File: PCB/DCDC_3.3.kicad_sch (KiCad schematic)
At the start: 16 parts, among them U10 LV2842XLVDDCR

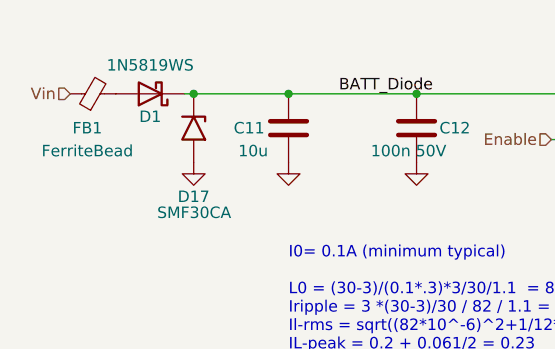
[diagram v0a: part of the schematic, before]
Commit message: Schootky reverse voltage protection replaced with switching diode to make there is no reverse current
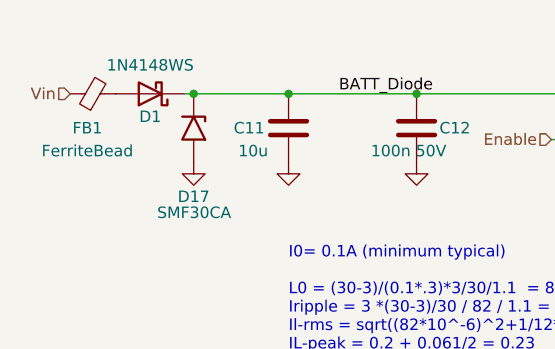
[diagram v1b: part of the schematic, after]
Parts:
- D1: value 1N5819WS -> 1N4148WS; LCSC C191023 -> C2128
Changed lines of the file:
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@@
       (effects (font (size 1.27 1.27)))
     )
-    (property "Value" "1N5819WS" (at 63.373 42.037 0)
+    (property "Value" "1N4148WS" (at 63.373 42.037 0)
       (effects (font (size 1.27 1.27)))
     )
@@
       (effects (font (size 1.27 1.27)) hide)
     )
-    (property "Datasheet" "https://datasheet.lcsc.com/lcsc/2204281430_Guangdong-Hottech-1N5819WS_C191023.pdf" (at 63.373 45.212 0)
+    (property "Datasheet" "https://datasheet.lcsc.com/lcsc/1810101110_Jiangsu-Changjing-Electronics-Technology-Co---Ltd--1N4148WS_C2128.pdf" (at 63.373 45.212 0)
       (effects (font (size 1.27 1.27)) hide)
     )
-    (property "LCSC" "C191023" (at 63.6905 38.227 0)
+    (property "LCSC" "C2128" (at 63.6905 38.227 0)
       (effects (font (size 1.27 1.27)) hide)
     )

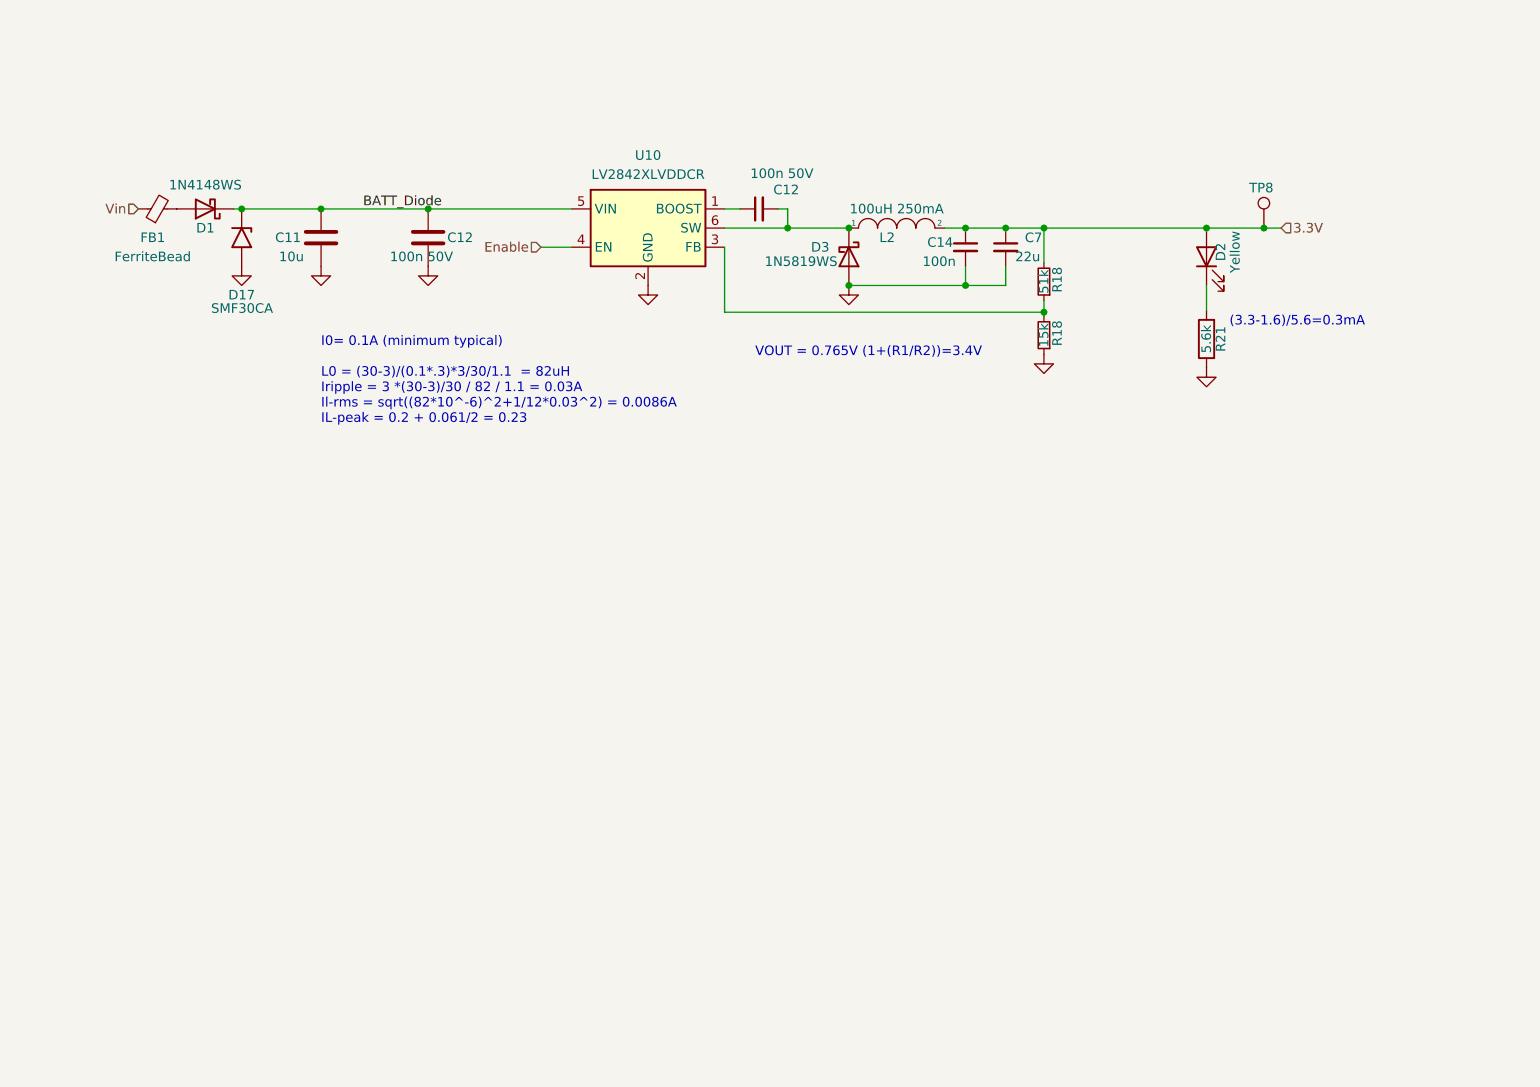
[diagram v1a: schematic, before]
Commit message: P-channel aux load switching pullup (normally opened). Optional disabling of DCDC
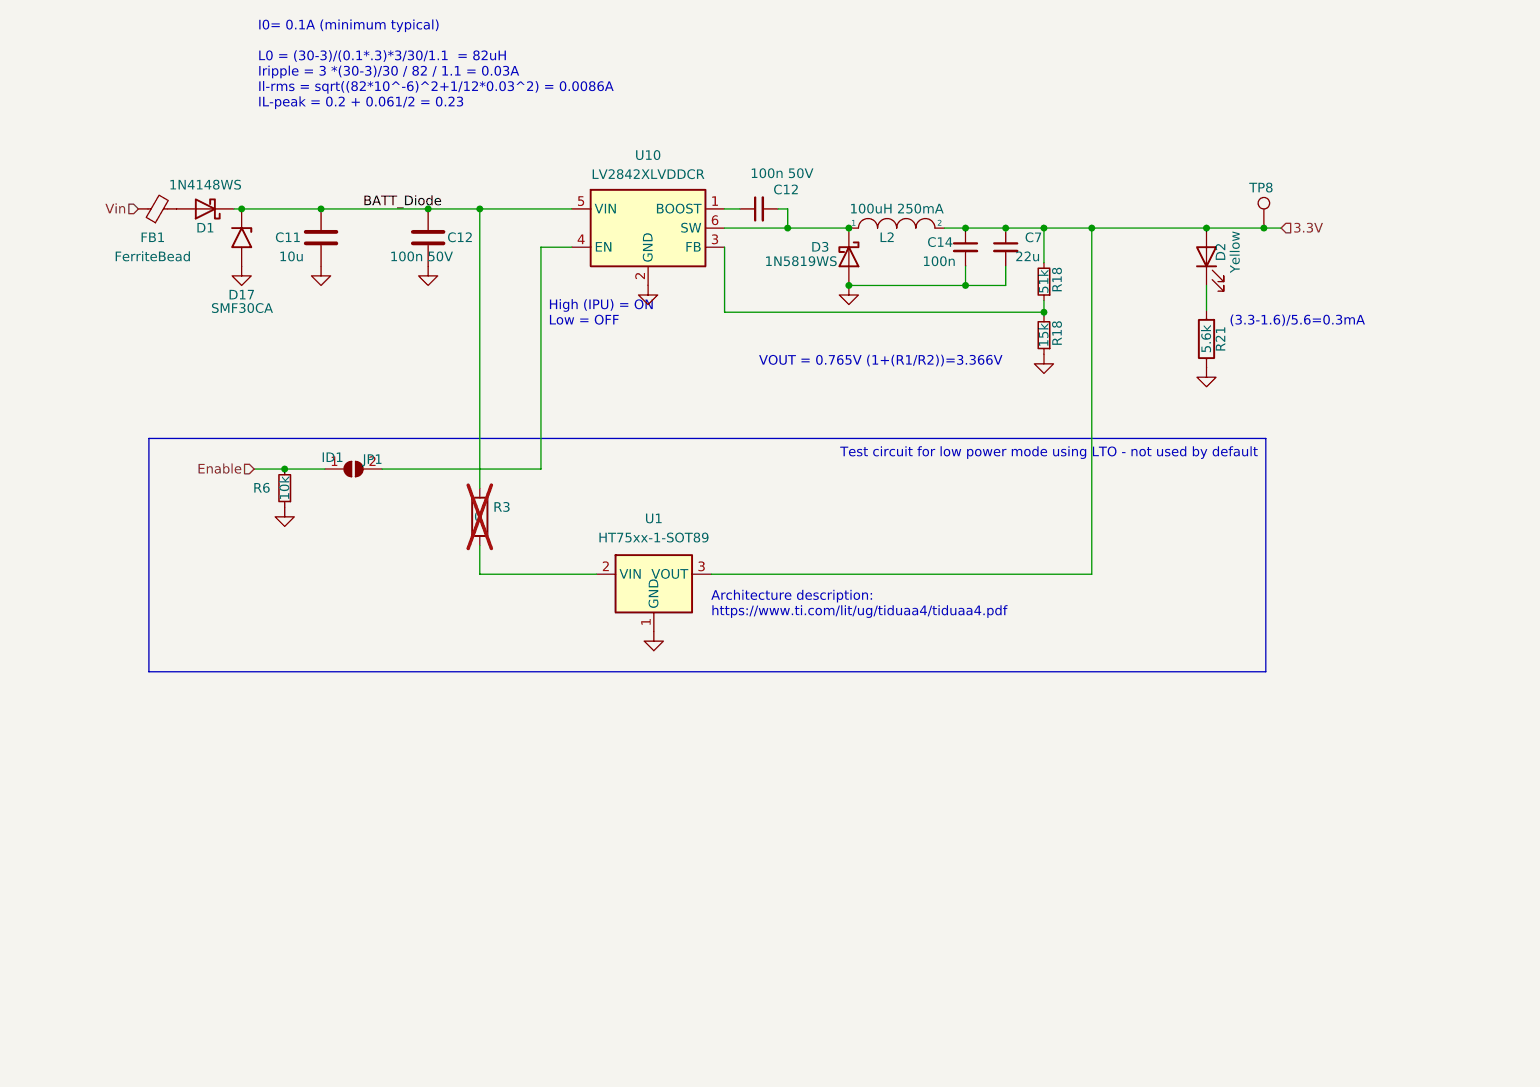
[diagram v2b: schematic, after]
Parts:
- added JP1: ID1, Jumper:SolderJumper-2_P1.3mm_Open_RoundedPad1.0x1.5mm, symbol Jumper:SolderJumper_2_Open
- added R3: 0, Resistor_SMD:R_0805_2012Metric, symbol Device:R
- added R6: 10k, Resistor_SMD:R_0402_1005Metric, symbol Device:R_Small
- added U1: HT75xx-1-SOT89, Package_TO_SOT_SMD:SOT-89-3, symbol Regulator_Linear:HT75xx-1-SOT89
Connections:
- net 3.3V: now also U1.3 (VOUT)
- net BATT_Diode: now also R3.1
- net Enable: now also JP1.1 (A), R6.2; no longer U10.4 (EN)
- net GND: now also R6.1, U1.1 (GND)
- new net: JP1.2 (B), U10.4 (EN)
- new net: R3.2, U1.2 (VIN)
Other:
- note added: "Architecture description: https://www.ti.com/lit/ug/tiduaa4/tiduaa4.pdf"
- note added: "High (IPU) = ON Low = OFF"
- note added: "VOUT = 0.765V (1+(R1/R2))=3.366V"
- note removed: "VOUT = 0.765V (1+(R1/R2))=3.4V"

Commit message: Mosfets for load switchiong. DCDC Enable pin. Rerouting.
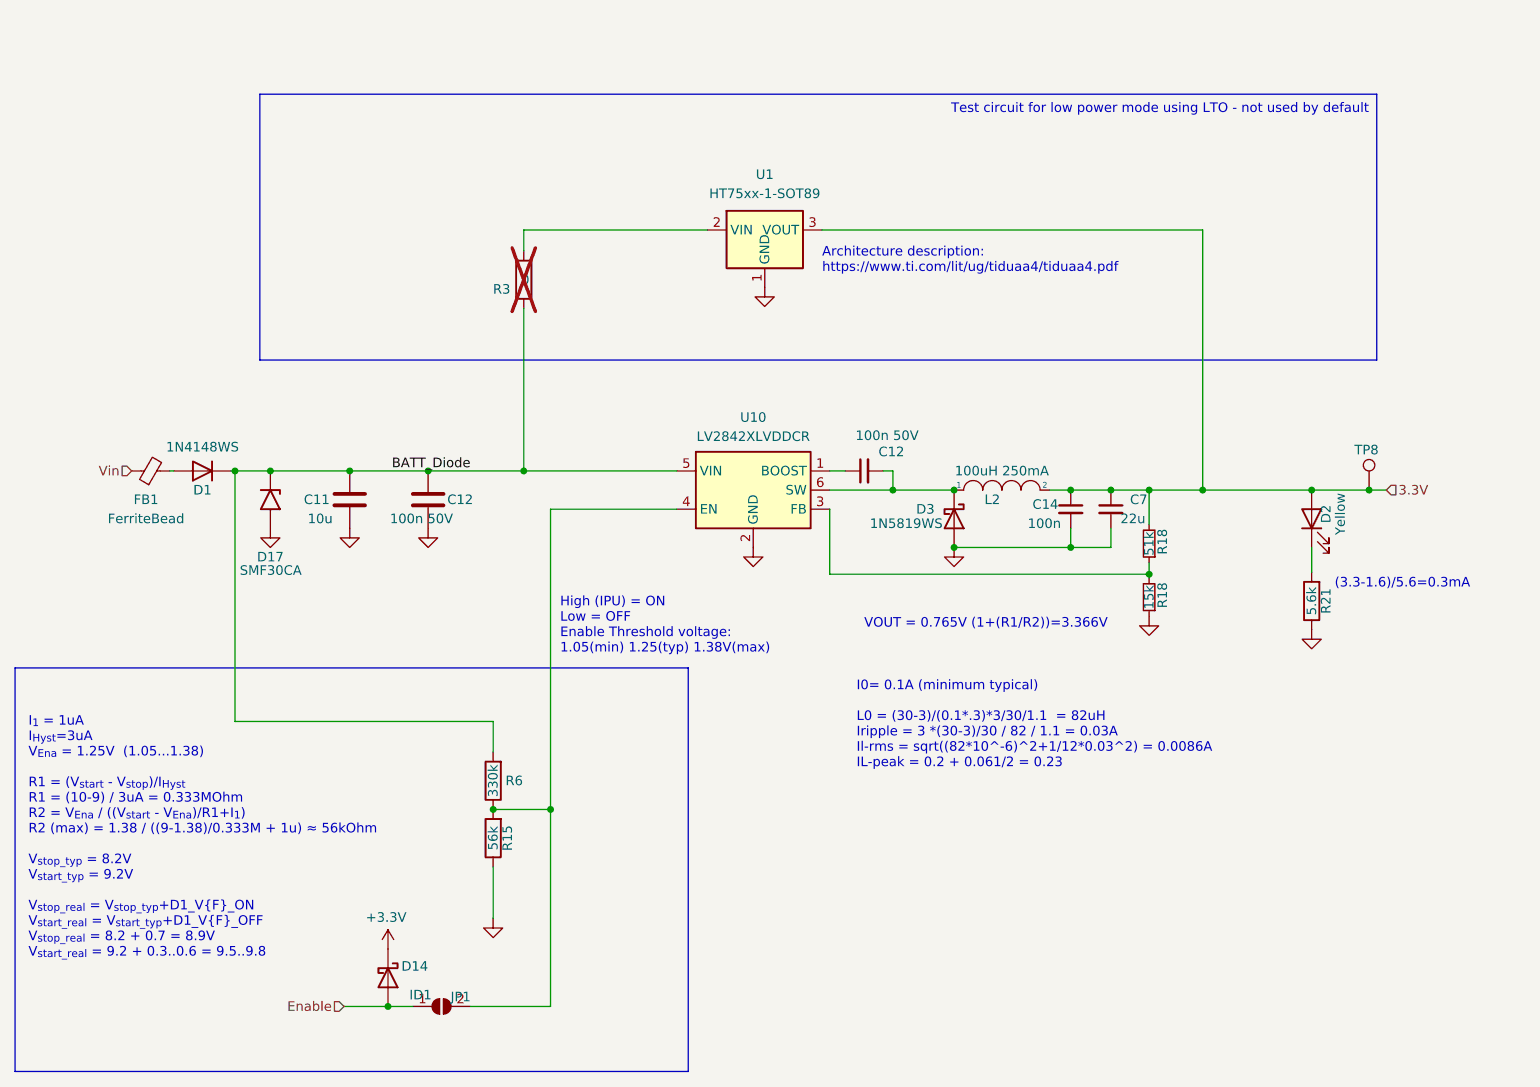
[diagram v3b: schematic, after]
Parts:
- removed R6: 10k, Resistor_SMD:R_0402_1005Metric, symbol Device:R_Small
- added D14: 1N5819WS, Diode_SMD:D_SOD-323, symbol Diode:1N5819
- added R15: 56k, Resistor_SMD:R_0402_1005Metric, symbol Device:R
- added R6: 330k, Resistor_SMD:R_0402_1005Metric, symbol Device:R
- D1: symbol Diode:1N5819 -> Diode:1N4148WS; Note (none) -> Low reverse current
- R3: LCSC (none) -> C21189; LSCS C21189 -> (none)
- U1: LCSC (none) -> C14289; LSCS C14289 -> (none)
- U10: Alternative LMR14010A or LMR14006 -> LMR14010A or LMR14006 or TPS54160; LCSC (none) -> C225807; LSCS C225807 -> (none)
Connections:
- net BATT_Diode: now also R6.2
- net Enable: now also D14.2 (A)
- net GND: now also R15.1
- net at JP1.2 (B), U10.4 (EN): now also R15.2, R6.1
- new net +3.3V: D14.1 (K)
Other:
- note added: "High (IPU) = ON Low = OFF Enable Threshold voltage: 1.05(min) 1.25(typ) 1.38V(max)"
- note added: "I_{1} = 1uA I_{Hyst}=3uA V_{Ena} = 1.25V (1.05...1.38) R1 = (V_{start} - V_{stop})/I_{Hyst} R1 = (10-9) / 3uA = 0.333MOhm R2 = V_{Ena} / ((V_{start} - V_{Ena})/R1+I_{1}) R2 (max) = 1.38 / ((9-1.38)/0.333M + 1u) ≈ 56kOhm V_{stop_typ} = 8.2V V_{start_typ} = 9.2V V_{stop_real} = V_{stop_typ}+D1_V{F}_ON V_{start_real} = V_{start_typ}+D1_V{F}_OFF V_{stop_real} = 8.2 + 0.7 = 8.9V V_{start_real} = 9.2 +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"
- note removed: "High (IPU) = ON Low = OFF"
- moved on the sheet: C11, C12, C14, C7, D1, D17, D2, D3, FB1, JP1, L2, R18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

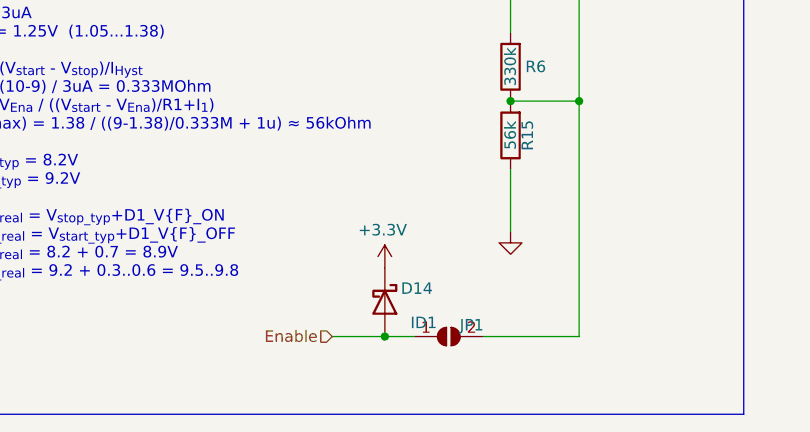
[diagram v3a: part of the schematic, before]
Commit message: DCDC force enable option
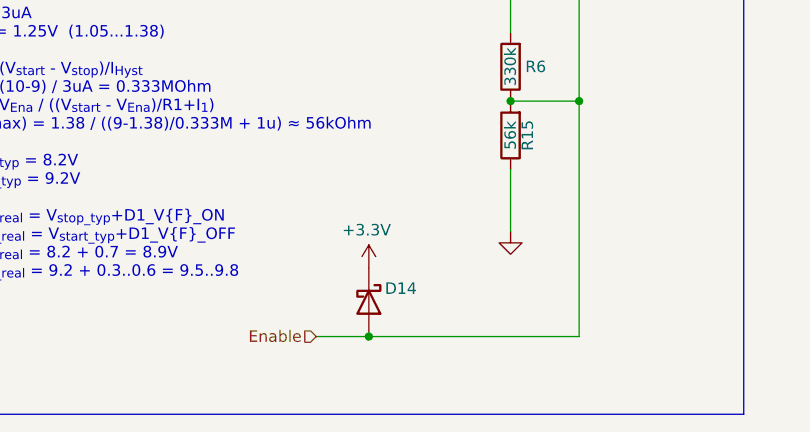
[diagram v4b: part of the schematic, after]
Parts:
- removed JP1: ID1, Jumper:SolderJumper-2_P1.3mm_Open_RoundedPad1.0x1.5mm, symbol Jumper:SolderJumper_2_Open
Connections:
- net Enable: now also R15.2, R6.1, U10.4 (EN)
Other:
- moved on the sheet: D14
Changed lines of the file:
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@@
   (junction (at 188.722 82.55) (diameter 0) (color 0 0 0 0)
   )
-  (junction (at 87.63 151.13) (diameter 0) (color 0 0 0 0)
+  (junction (at 85.852 151.13) (diameter 0) (color 0 0 0 0)
   )
   (junction (at 101.6 124.968) (diameter 0) (color 0 0 0 0)
@@
     (stroke (width 0) (type default))
   )
-  (wire (pts (xy 81.788 151.13) (xy 87.63 151.13))
+  (wire (pts (xy 80.01 151.13) (xy 85.852 151.13))
     (stroke (width 0) (type default))
   )
@@
     (stroke (width 0) (type default))
   )
-  (wire (pts (xy 87.63 151.13) (xy 90.932 151.13))
-    (stroke (width 0) (type default))
-  )
   (wire (pts (xy 153.416 80.01) (xy 154.686 80.01))
     (stroke (width 0) (type default))
@@
     (stroke (width 0) (type default))
   )
-  (wire (pts (xy 98.552 151.13) (xy 109.22 151.13))
+  (wire (pts (xy 85.852 151.13) (xy 109.22 151.13))
     (stroke (width 0) (type default))
   )
@@
     (effects (font (size 1.27 1.27)) (justify left))
   )
-  (hierarchical_label "Enable" (shape input) (at 81.788 151.13 180) (fields_autoplaced)
+  (hierarchical_label "Enable" (shape input) (at 80.01 151.13 180) (fields_autoplaced)
     (effects (font (size 1.27 1.27)) (justify right))
   )
@@
     )
   )
-  (symbol (lib_id "Diode:1N5819") (at 87.63 147.32 270) (unit 1)
-    (in_bom yes) (on_board yes) (dnp no)
-    (property "Reference" "D14" (at 91.186 145.796 90)
-      (effects (font (size 1.27 1.27)))
-    )
-    (property "Value" "1N5819WS" (at 94.234 147.828 90)
-      (effects (font (size 1.27 1.27)) hide)
-    )
-    (property "Footprint" "Diode_SMD:D_SOD-323" (at 83.185 147.32 0)
-      (effects (font (size 1.27 1.27)) hide)
-    )
-    (property "Datasheet" "https://datasheet.lcsc.com/lcsc/2204281430_Guangdong-Hottech-1N5819WS_C191023.pdf" (at 87.63 147.32 0)
-      (effects (font (size 1.27 1.27)) hide)
-    )
-    (property "LCSC" "C191023" (at 80.645 147.0025 0)
+  (symbol (lib_id "Diode:1N5819") (at 85.852 147.32 270) (unit 1)
+    (in_bom yes) (on_board yes) (dnp no)
+    (property "Reference" "D14" (at 89.408 145.796 90)
+      (effects (font (size 1.27 1.27)))
+    )
+    (property "Value" "1N5819WS" (at 92.456 147.828 90)
+      (effects (font (size 1.27 1.27)) hide)
+    )
+    (property "Footprint" "Diode_SMD:D_SOD-323" (at 81.407 147.32 0)
+      (effects (font (size 1.27 1.27)) hide)
+    )
+    (property "Datasheet" "https://datasheet.lcsc.com/lcsc/2204281430_Guangdong-Hottech-1N5819WS_C191023.pdf" (at 85.852 147.32 0)
+      (effects (font (size 1.27 1.27)) hide)
+    )
+    (property "LCSC" "C191023" (at 78.867 147.0025 0)
       (effects (font (size 1.27 1.27)) hide)
     )
@@
     )
   )
-  (symbol (lib_id "Jumper:SolderJumper_2_Open") (at 94.742 151.13 0) (unit 1)
-    (in_bom yes) (on_board yes) (dnp no)
-    (property "Reference" "JP1" (at 97.282 149.86 0)
-      (effects (font (size 1.27 1.27)))
-    )
-    (property "Value" "ID1" (at 91.948 149.606 0)
-      (effects (font (size 1.27 1.27)))
-    )
-    (property "Footprint" "Jumper:SolderJumper-2_P1.3mm_Open_RoundedPad1.0x1.5mm" (at 94.742 151.13 0)
-      (effects (font (size 1.27 1.27)) hide)
-    )
-    (property "Datasheet" "~" (at 94.742 151.13 0)
-      (effects (font (size 1.27 1.27)) hide)
-    )
-    (pin "1")
-    (pin "2")
-    (instances
-      (project "StepperServoCAN"
-        (path "/92dad13e-412a-43d4-9260-9087579302b1"
-          (reference "JP1") (unit 1)
-        )
-        (path "/92dad13e-412a-43d4-9260-9087579302b1/82f027ad-2d00-453d-ab1c-0ba3b5cb1ef7"
-          (reference "JP5") (unit 1)
-        )
-      )
-    )
-  )
   (symbol (lib_id "power:GND") (at 101.6 139.446 0) (unit 1)
     (in_bom yes) (on_board yes) (dnp no)
@@
     )
   )
-  (symbol (lib_id "power:+3.3V") (at 87.63 143.51 0) (unit 1)
-    (in_bom yes) (on_board yes) (dnp no)
-    (property "Reference" "#PWR06" (at 87.63 147.32 0)
-      (effects (font (size 1.27 1.27)) hide)
-    )
-    (property "Value" "+3.3V" (at 87.3819 139.3021 0)
-      (effects (font (size 1.27 1.27)))
-    )
-    (property "Footprint" "" (at 87.63 143.51 0)
-      (effects (font (size 1.27 1.27)) hide)
-    )
-    (property "Datasheet" "" (at 87.63 143.51 0)
-      (effects (font (size 1.27 1.27)) hide)
-    )
+  (symbol (lib_id "power:+3.3V") (at 85.852 143.51 0) (unit 1)
+    (in_bom yes) (on_board yes) (dnp no)
+    (property "Reference" "#PWR06" (at 85.852 147.32 0)
+      (effects (font (size 1.27 1.27)) hide)
+    )
+    (property "Value" "+3.3V" (at 85.6039 139.3021 0)
+      (effects (font (size 1.27 1.27)))
+    )
+    (property "Footprint" "" (at 85.852 143.51 0)
+      (effects (font (size 1.27 1.27)) hide)
+    )
+    (property "Datasheet" "" (at 85.852 143.51 0)
+      (effects (font (size 1.27 1.27)) hide)
+    )
